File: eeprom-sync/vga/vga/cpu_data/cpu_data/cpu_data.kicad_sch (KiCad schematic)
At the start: 26 parts, among them J1 Conn_01x06_Female, J10 Conn_01x03_Female, J11 Conn_01x02_Female, J2 Conn_01x02_Female, J3 Conn_01x04_Female, J4 Conn_01x15_Female, J5 Conn_01x15_Female, J6 Conn_01x08_Female, J7 Conn_01x02_Female, J8 Conn_01x02_Female, J9 Conn_01x08_Female, U1 GAL22V10, U2 SN74ACT08, U3 74HC273

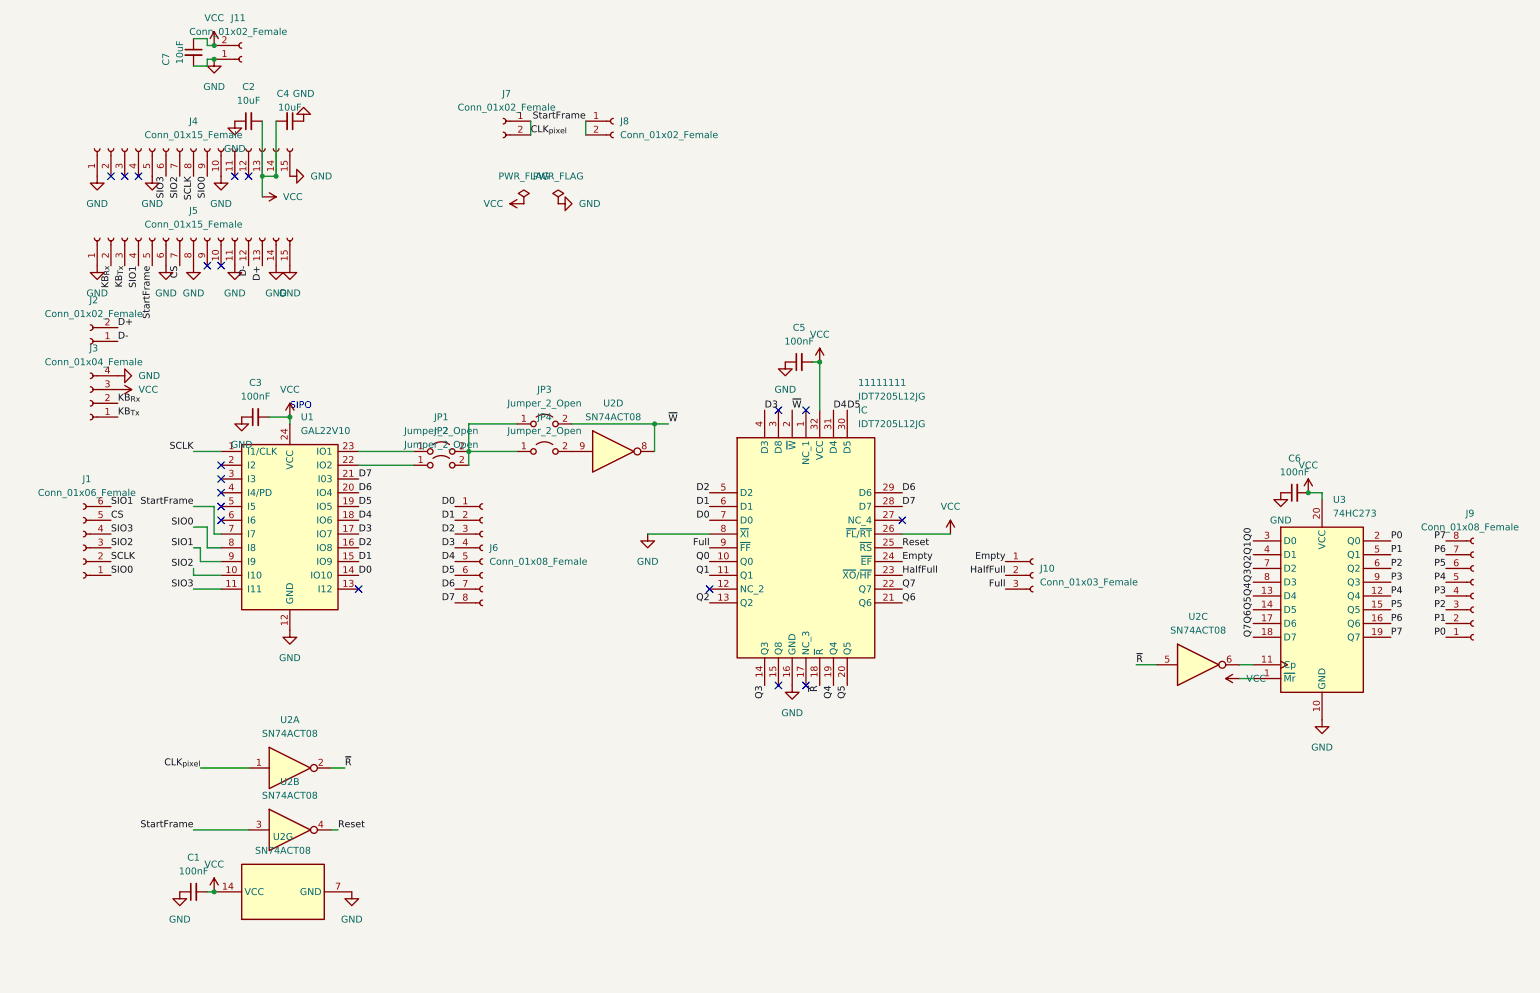
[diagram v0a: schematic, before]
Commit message: cpu data now uses RC circuits for timing instead of not gates
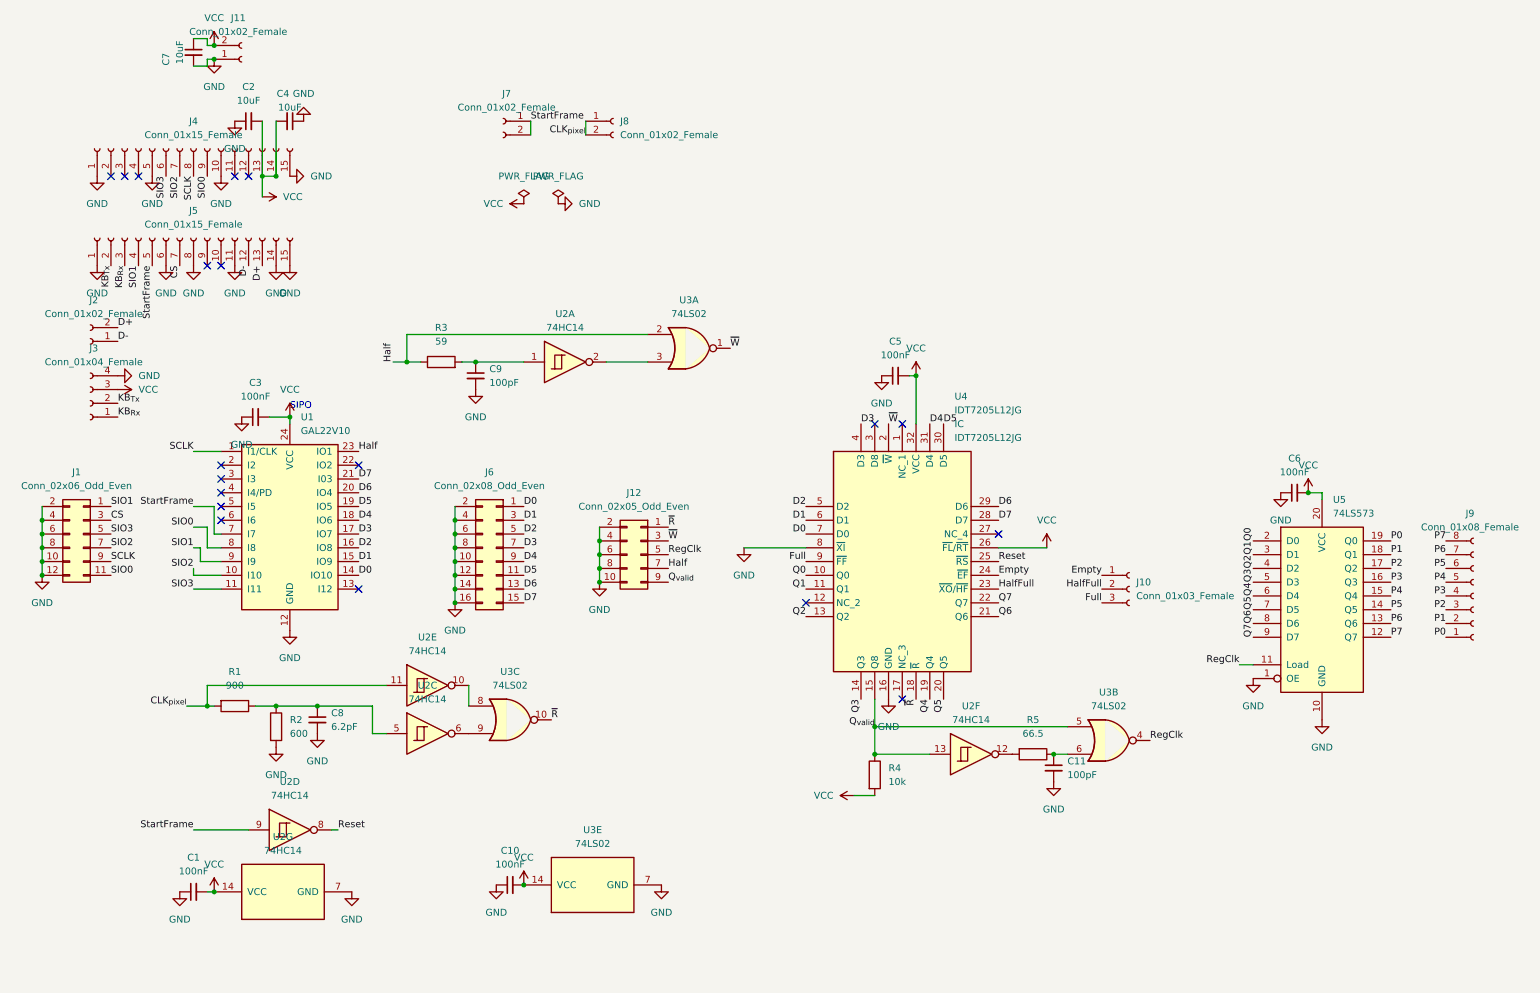
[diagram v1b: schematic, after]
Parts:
- removed J1: Conn_01x06_Female, Connector_PinSocket_2.54mm:PinSocket_1x06_P2.54mm_Vertical, symbol Connector:Conn_01x06_Female
- removed J6: Conn_01x08_Female, Connector_PinSocket_2.54mm:PinSocket_1x08_P2.54mm_Vertical, symbol Connector:Conn_01x08_Female
- removed JP1, JP2, JP3, JP4: Jumper_2_Open, TestPoint:TestPoint_2Pads_Pitch2.54mm_Drill0.8mm, symbol Jumper:Jumper_2_Open
- removed U2: SN74ACT08, Package_SO:SOIC-14_3.9x8.7mm_P1.27mm, symbol 74xx:74LS04
- removed U3: 74HC273, Package_SO:SO-20_12.8x7.5mm_P1.27mm, symbol 74xx:74HC273
- added C10: 100nF, Capacitor_SMD:C_0603_1608Metric_Pad1.08x0.95mm_HandSolder, symbol Device:C_Small
- added C11, C9: 100pF, Capacitor_SMD:C_0603_1608Metric, symbol Device:C_Small
- added C8: 6.2pF, Capacitor_SMD:C_0603_1608Metric, symbol Device:C_Small
- added J1: Conn_02x06_Odd_Even, Connector_PinHeader_2.54mm:PinHeader_2x06_P2.54mm_Vertical, symbol Connector_Generic:Conn_02x06_Odd_Even
- added J12: Conn_02x05_Odd_Even, Connector_PinHeader_2.54mm:PinHeader_2x05_P2.54mm_Vertical, symbol Connector_Generic:Conn_02x05_Odd_Even
- added J6: Conn_02x08_Odd_Even, Connector_PinHeader_2.54mm:PinHeader_2x08_P2.54mm_Vertical, symbol Connector_Generic:Conn_02x08_Odd_Even
- added R1: 900, Resistor_SMD:R_0805_2012Metric_Pad1.20x1.40mm_HandSolder, symbol Device:R
- added R2: 600, Resistor_SMD:R_0805_2012Metric_Pad1.20x1.40mm_HandSolder, symbol Device:R
- added R3: 59, Resistor_SMD:R_0805_2012Metric_Pad1.20x1.40mm_HandSolder, symbol Device:R
- added R4: 10k, Resistor_SMD:R_0805_2012Metric_Pad1.20x1.40mm_HandSolder, symbol Device:R
- added R5: 66.5, Resistor_SMD:R_0805_2012Metric_Pad1.20x1.40mm_HandSolder, symbol Device:R
- added U2: 74HC14, Package_SO:SOIC-14_3.9x8.7mm_P1.27mm, symbol 74xx:74HC14
- added U3: 74LS02, Package_SO:SOIC-14_3.9x8.7mm_P1.27mm, symbol 74xx:74LS02
- added U5: 74LS573, Package_SO:SOIC-20W_7.5x15.4mm_P1.27mm, symbol 74xx:74LS573
- U4: renamed from 11111111; Product (none) -> https://www.jameco.com/z/69802-032-Amphenol-Socket-PLCC-32-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
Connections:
- net CLK_{pixel}: now also J8.1 (Pin_1), J8.2 (Pin_2), R1.2, U2.11; no longer J7.1 (Pin_1), J7.2 (Pin_2)
- net CS: now also J1.3 (Pin_3)
- net D0: now also J6.1 (Pin_1)
- net D1: now also J6.3 (Pin_3)
- net D2: now also J6.5 (Pin_5)
- net D3: now also J6.7 (Pin_7)
- net D4: now also J6.9 (Pin_9)
- net D5: now also J6.11 (Pin_11)
- net D6: now also J6.13 (Pin_13)
- net D7: now also J6.15 (Pin_15)
- net GND: now also C10.1, C11.2, C8.2, C9.2, J1.10 (Pin_10), J1.12 (Pin_12), J1.2 (Pin_2), J1.4 (Pin_4), J1.6 (Pin_6), J1.8 (Pin_8), J12.10 (Pin_10), J12.2 (Pin_2), J12.4 (Pin_4), J12.6 (Pin_6), J12.8 (Pin_8), J6.10 (Pin_10), J6.12 (Pin_12), J6.14 (Pin_14), J6.16 (Pin_16), J6.2 (Pin_2), J6.4 (Pin_4), J6.6 (Pin_6), J6.8 (Pin_8), R2.2, U2.7 (GND), U3.7 (GND), U5.1 (OE), U5.10 (GND)
- net KB_{Rx}: now also J3.1 (Pin_1), J5.3 (Pin_3); no longer J3.2 (Pin_2), J5.2 (Pin_2)
- net KB_{Tx}: now also J3.2 (Pin_2), J5.2 (Pin_2); no longer J3.1 (Pin_1), J5.3 (Pin_3)
- net P0: now also U5.19 (Q0)
- net P1: now also U5.18 (Q1)
- net P2: now also U5.17 (Q2)
- net P3: now also U5.16 (Q3)
- net P4: now also U5.15 (Q4)
- net P5: now also U5.14 (Q5)
- net P6: now also U5.13 (Q6)
- net P7: now also U5.12 (Q7)
- net Q0: now also U5.2 (D0)
- net Q1: now also U5.3 (D1)
- net Q2: now also U5.4 (D2)
- net Q3: now also U5.5 (D3)
- net Q4: now also U5.6 (D4)
- net Q5: now also U5.7 (D5)
- net Q6: now also U5.8 (D6)
- net Q7: now also U5.9 (D7)
- net Reset: now also U2.8
- net SCLK: now also J1.9 (Pin_9)
- net SIO0: now also J1.11 (Pin_11)
- net SIO1: now also J1.1 (Pin_1)
- net SIO2: now also J1.7 (Pin_7)
- net SIO3: now also J1.5 (Pin_5)
- net StartFrame: now also J7.1 (Pin_1), J7.2 (Pin_2), U2.9; no longer J8.1 (Pin_1), J8.2 (Pin_2)
- net VCC: now also C10.2, R4.2, U2.14 (VCC), U3.14 (VCC), U5.20 (VCC)
- net ~{R}: now also J12.1 (Pin_1), U3.10
- net ~{W}: now also J12.3 (Pin_3), U3.1
- net Q_{valid}: now reaches U4.15 (Q8)
- net Q_{valid}: now also J12.9 (Pin_9), R4.1, U2.13, U3.5
- net Half: now reaches U1.23 (IO1)
- net Half: now also J12.7 (Pin_7), R3.1, U3.2
- new net: C8.1, R1.1, R2.1, U2.5
- new net: U2.10, U3.8
- new net: U2.6, U3.9
- new net: C9.1, R3.2, U2.1
- new net: C11.1, R5.1, U3.6
- new net: U2.2, U3.3
- new net: R5.2, U2.12
- new net RegClk: J12.5 (Pin_5), U3.4, U5.11 (Load)
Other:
- moved on the sheet: C5, J10, U4

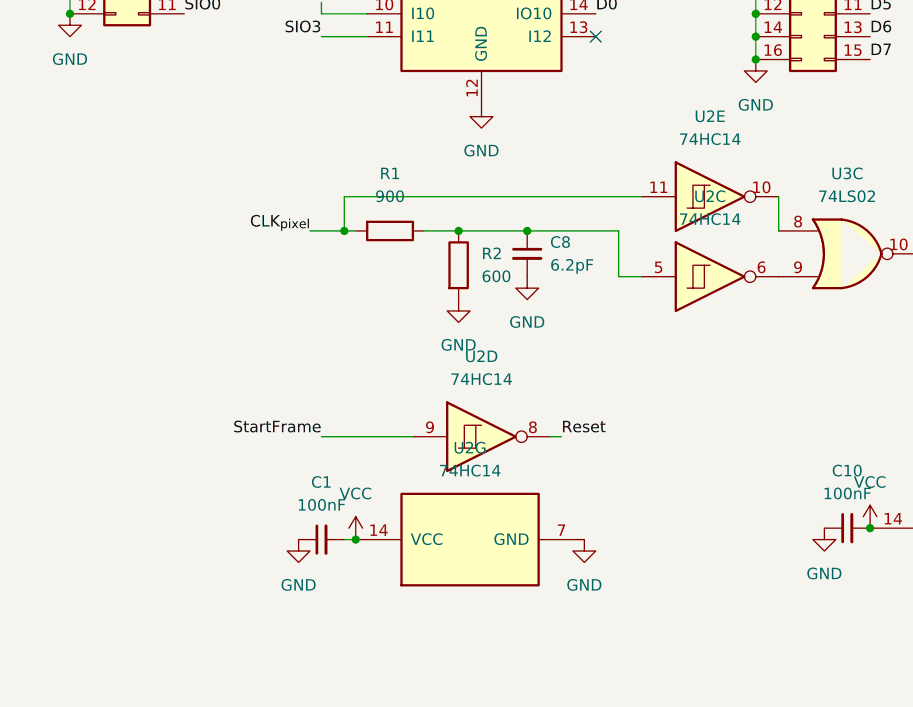
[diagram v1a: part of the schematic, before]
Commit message: cpu data board has transistor included
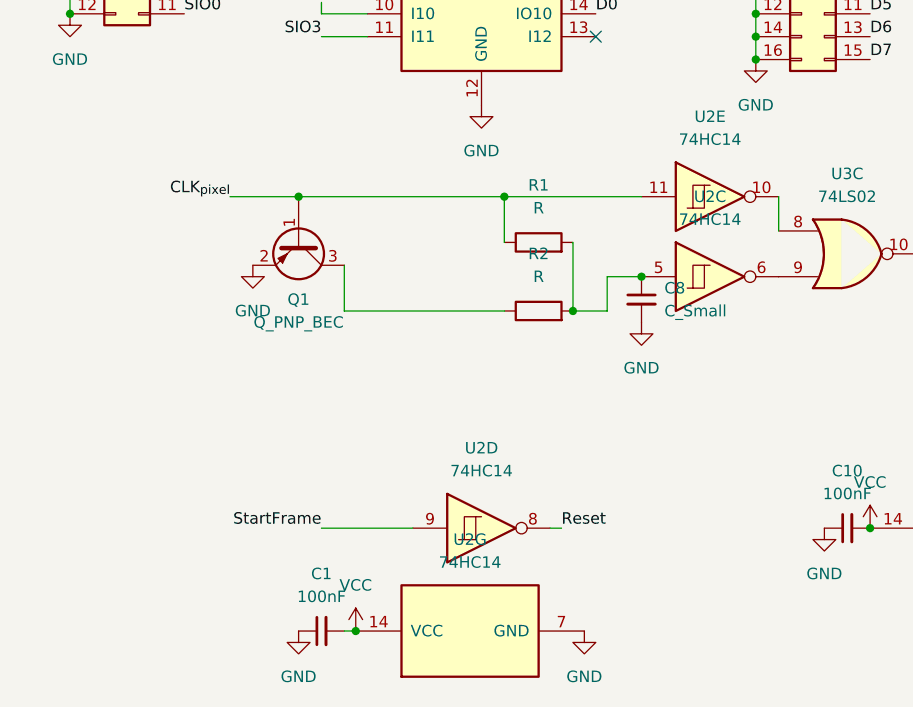
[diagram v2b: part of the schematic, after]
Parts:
- added Q1: Q_PNP_BEC, Package_TO_SOT_SMD:SOT-323_SC-70_Handsoldering, symbol Device:Q_PNP_BEC
- C8: value 6.2pF -> C_Small; footprint Capacitor_SMD:C_0603_1608Metric -> Capacitor_SMD:C_0603_1608Metric_Pad1.08x0.95mm_HandSolder; Product https://www.mouser.com/ProductDetail/Samsung-Electro-Mechan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 -> (none)
- J2: footprint Connector_PinSocket_2.54mm:PinSocket_1x02_P2.54mm_Vertical -> Connector_PinHeader_2.54mm:PinHeader_1x02_P2.54mm_Vertical
- R1: value 900 -> R
- R2: value 600 -> R
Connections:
- net CLK_{pixel}: now also R1.1, Q1.1 (B); no longer R1.2
- net GND: now also Q1.2 (E); no longer R2.2
- net at C8.1, U2.5: now also R1.2, R2.2; no longer R1.1, R2.1
- new net: Q1.3 (C), R2.1
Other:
- moved on the sheet: C1, U2D, U2G

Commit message: finalized form of pcb and schematic
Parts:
- removed Q1: Q_PNP_BEC, Package_TO_SOT_SMD:SOT-323_SC-70_Handsoldering, symbol Device:Q_PNP_BEC
- removed R2: R, Resistor_SMD:R_0805_2012Metric_Pad1.20x1.40mm_HandSolder, symbol Device:R
- removed unit 5 of U2
- removed unit 3 of U2
- added Q1: Q_PMOS_GSD, Package_TO_SOT_SMD:SOT-323_SC-70_Handsoldering, symbol Device:Q_PMOS_GSD
- C8: value C_Small -> 24pF; Product (none) -> https://www.mouser.com/ProductDetail/KEMET/C0603C240G1HACTU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
- U3: Product (none) -> https://www.mouser.com/ProductDetail/Texas-Instruments/SN74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
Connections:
- net CLK_{pixel}: now also U3.8, Q1.1 (G)
- net VCC: now also Q1.3 (D)
- net at C8.1, R1.2: now also U3.9, Q1.2 (S)
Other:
- moved on the sheet: C8, U3C

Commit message: retracing some lines and taking out several vias, making all smd caps and Rs to be the same footprint size
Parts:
- C1, C10, C3, C5, C6, C8: footprint Capacitor_SMD:C_0603_1608Metric_Pad1.08x0.95mm_HandSolder -> Capacitor_SMD:C_0805_2012Metric_Pad1.18x1.45mm_HandSolder
- C11, C9: footprint Capacitor_SMD:C_0603_1608Metric -> Capacitor_SMD:C_0805_2012Metric_Pad1.18x1.45mm_HandSolder
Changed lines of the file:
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@@
     (property "Reference" "C5" (id 0) (at 171.4563 72.39 90))
     (property "Value" "100nF" (id 1) (at 171.4563 74.93 90))
-    (property "Footprint" "Capacitor_SMD:C_0603_1608Metric_Pad1.08x0.95mm_HandSolder" (id 2) (at 171.45 78.74 0)
+    (property "Footprint" "Capacitor_SMD:C_0805_2012Metric_Pad1.18x1.45mm_HandSolder" (id 2) (at 171.45 78.74 0)
       (effects (font (size 1.27 1.27)) hide)
     )
@@
       (effects (font (size 1.27 1.27)) (justify left))
     )
-    (property "Footprint" "Capacitor_SMD:C_0603_1608Metric_Pad1.08x0.95mm_HandSolder" (id 2) (at 63.5 149.86 0)
+    (property "Footprint" "Capacitor_SMD:C_0805_2012Metric_Pad1.18x1.45mm_HandSolder" (id 2) (at 63.5 149.86 0)
       (effects (font (size 1.27 1.27)) hide)
     )
@@
     (property "Reference" "C10" (id 0) (at 100.3363 166.37 90))
     (property "Value" "100nF" (id 1) (at 100.3363 168.91 90))
-    (property "Footprint" "Capacitor_SMD:C_0603_1608Metric_Pad1.08x0.95mm_HandSolder" (id 2) (at 100.33 172.72 0)
+    (property "Footprint" "Capacitor_SMD:C_0805_2012Metric_Pad1.18x1.45mm_HandSolder" (id 2) (at 100.33 172.72 0)
       (effects (font (size 1.27 1.27)) hide)
     )
@@
     (property "Reference" "C1" (id 0) (at 41.9163 177.8 90))
     (property "Value" "100nF" (id 1) (at 41.9163 180.34 90))
-    (property "Footprint" "Capacitor_SMD:C_0603_1608Metric_Pad1.08x0.95mm_HandSolder" (id 2) (at 41.91 184.15 0)
+    (property "Footprint" "Capacitor_SMD:C_0805_2012Metric_Pad1.18x1.45mm_HandSolder" (id 2) (at 41.91 184.15 0)
       (effects (font (size 1.27 1.27)) hide)
     )
@@
     (property "Reference" "C3" (id 0) (at 53.3463 80.01 90))
     (property "Value" "100nF" (id 1) (at 53.3463 82.55 90))
-    (property "Footprint" "Capacitor_SMD:C_0603_1608Metric_Pad1.08x0.95mm_HandSolder" (id 2) (at 53.34 86.36 0)
+    (property "Footprint" "Capacitor_SMD:C_0805_2012Metric_Pad1.18x1.45mm_HandSolder" (id 2) (at 53.34 86.36 0)
       (effects (font (size 1.27 1.27)) hide)
     )
@@
       (effects (font (size 1.27 1.27)) (justify left))
     )
-    (property "Footprint" "Capacitor_SMD:C_0603_1608Metric" (id 2) (at 200.66 151.13 0)
+    (property "Footprint" "Capacitor_SMD:C_0805_2012Metric_Pad1.18x1.45mm_HandSolder" (id 2) (at 200.66 151.13 0)
       (effects (font (size 1.27 1.27)) hide)
     )
@@
     (property "Reference" "C6" (id 0) (at 245.1163 93.98 90))
     (property "Value" "100nF" (id 1) (at 245.1163 96.52 90))
-    (property "Footprint" "Capacitor_SMD:C_0603_1608Metric_Pad1.08x0.95mm_HandSolder" (id 2) (at 245.11 100.33 0)
+    (property "Footprint" "Capacitor_SMD:C_0805_2012Metric_Pad1.18x1.45mm_HandSolder" (id 2) (at 245.11 100.33 0)
       (effects (font (size 1.27 1.27)) hide)
     )
@@
       (effects (font (size 1.27 1.27)) (justify left))
     )
-    (property "Footprint" "Capacitor_SMD:C_0603_1608Metric" (id 2) (at 93.98 78.74 0)
+    (property "Footprint" "Capacitor_SMD:C_0805_2012Metric_Pad1.18x1.45mm_HandSolder" (id 2) (at 93.98 78.74 0)
       (effects (font (size 1.27 1.27)) hide)
     )
@@
     )
     (path "/6d97fa49-1c40-4588-b114-7b816ee2ddf7"
-      (reference "C1") (unit 1) (value "100nF") (footprint "Capacitor_SMD:C_0603_1608Metric_Pad1.08x0.95mm_HandSolder")
+      (reference "C1") (unit 1) (value "100nF") (footprint "Capacitor_SMD:C_0805_2012Metric_Pad1.18x1.45mm_HandSolder")
     )
     (path "/7b7af9e5-d7e0-45e7-8bd0-0c6327302689"
@@
     )
     (path "/74b15c23-64fb-4b0d-a247-7ccfe0bd3167"
-      (reference "C3") (unit 1) (value "100nF") (footprint "Capacitor_SMD:C_0603_1608Metric_Pad1.08x0.95mm_HandSolder")
+      (reference "C3") (unit 1) (value "100nF") (footprint "Capacitor_SMD:C_0805_2012Metric_Pad1.18x1.45mm_HandSolder")
     )
     (path "/9777a4f9-03e4-4209-95f0-6020ad67d6b2"
@@
     )
     (path "/2005d5e1-a683-4052-b118-2566f4f0cde3"
-      (reference "C5") (unit 1) (value "100nF") (footprint "Capacitor_SMD:C_0603_1608Metric_Pad1.08x0.95mm_HandSolder")
+      (reference "C5") (unit 1) (value "100nF") (footprint "Capacitor_SMD:C_0805_2012Metric_Pad1.18x1.45mm_HandSolder")
     )
     (path "/e4564e14-c354-4bcf-b2c0-93b271811638"
-      (reference "C6") (unit 1) (value "100nF") (footprint "Capacitor_SMD:C_0603_1608Metric_Pad1.08x0.95mm_HandSolder")
+      (reference "C6") (unit 1) (value "100nF") (footprint "Capacitor_SMD:C_0805_2012Metric_Pad1.18x1.45mm_HandSolder")
     )
     (path "/d78e83ca-90d0-4445-99d4-81ac1d6792ec"
@@
     )
     (path "/23b8c23a-2853-40c3-a53a-30fd914fa018"
-      (reference "C8") (unit 1) (value "24pF") (footprint "Capacitor_SMD:C_0603_1608Metric_Pad1.08x0.95mm_HandSolder")
+      (reference "C8") (unit 1) (value "24pF") (footprint "Capacitor_SMD:C_0805_2012Metric_Pad1.18x1.45mm_HandSolder")
     )
     (path "/e850d6f1-a8bd-462e-82e0-c6796e269fa2"
-      (reference "C9") (unit 1) (value "100pF") (footprint "Capacitor_SMD:C_0603_1608Metric")
+      (reference "C9") (unit 1) (value "100pF") (footprint "Capacitor_SMD:C_0805_2012Metric_Pad1.18x1.45mm_HandSolder")
     )
     (path "/3ef1ad17-6ee0-43b2-91af-599d89f98033"
-      (reference "C10") (unit 1) (value "100nF") (footprint "Capacitor_SMD:C_0603_1608Metric_Pad1.08x0.95mm_HandSolder")
+      (reference "C10") (unit 1) (value "100nF") (footprint "Capacitor_SMD:C_0805_2012Metric_Pad1.18x1.45mm_HandSolder")
     )
     (path "/a5a499f7-2cdb-4252-aa29-43aff812c464"
-      (reference "C11") (unit 1) (value "100pF") (footprint "Capacitor_SMD:C_0603_1608Metric")
+      (reference "C11") (unit 1) (value "100pF") (footprint "Capacitor_SMD:C_0805_2012Metric_Pad1.18x1.45mm_HandSolder")
     )
     (path "/1d866d70-1693-4c7b-b12b-14a1359fc1d5"

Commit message: adding the socket  footprint
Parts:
- removed Q1: Q_PMOS_GSD, Package_TO_SOT_SMD:SOT-323_SC-70_Handsoldering, symbol Device:Q_PMOS_GSD
- removed unit 3 of U3
- added unit 3 of U2
- added unit 5 of U2
- C8: value 24pF -> 100pF; Product https://www.mouser.com/ProductDetail/KEMET/C0603C240G1HACTU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 -> (none)
- U4: footprint Package_LCC:PLCC-32_11.4x14.0mm_P1.27mm -> plcc32:plcc32-socket
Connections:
- net ~{R}: now also J12.3 (Pin_3), U2.6; no longer J12.1 (Pin_1)
- net ~{W}: now also J12.1 (Pin_1), U2.10; no longer J12.3 (Pin_3), U3.1
- net at C8.1, R1.2: now also U2.5
- new net: U2.11, U3.1
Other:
- moved on the sheet: C8
